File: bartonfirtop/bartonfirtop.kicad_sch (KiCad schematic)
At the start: 3 parts

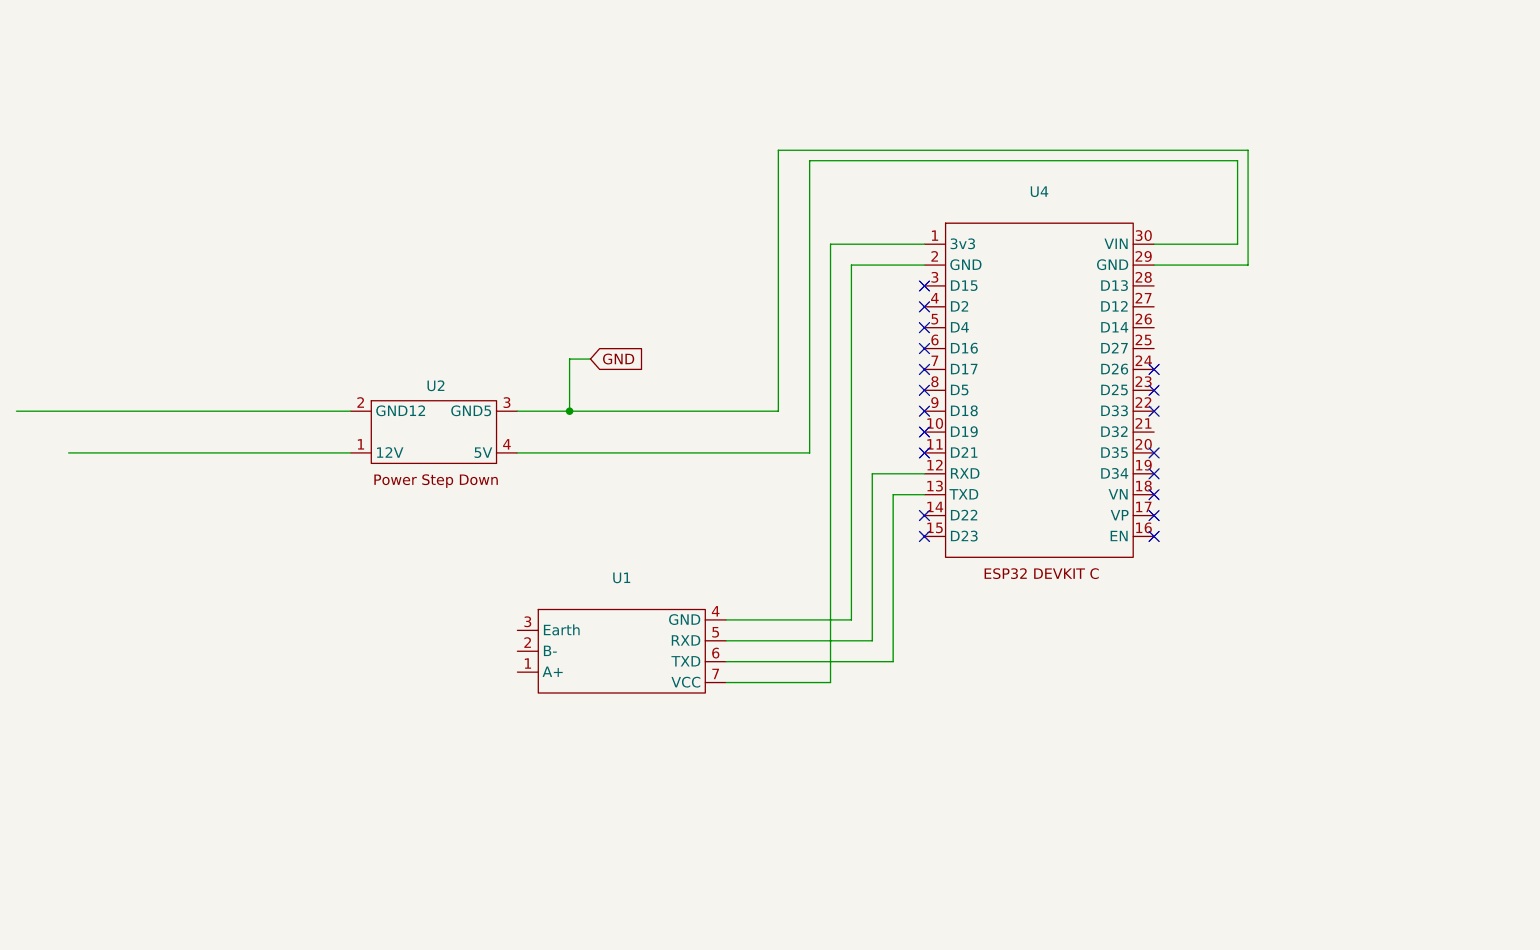
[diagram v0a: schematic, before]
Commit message: added LED connectors
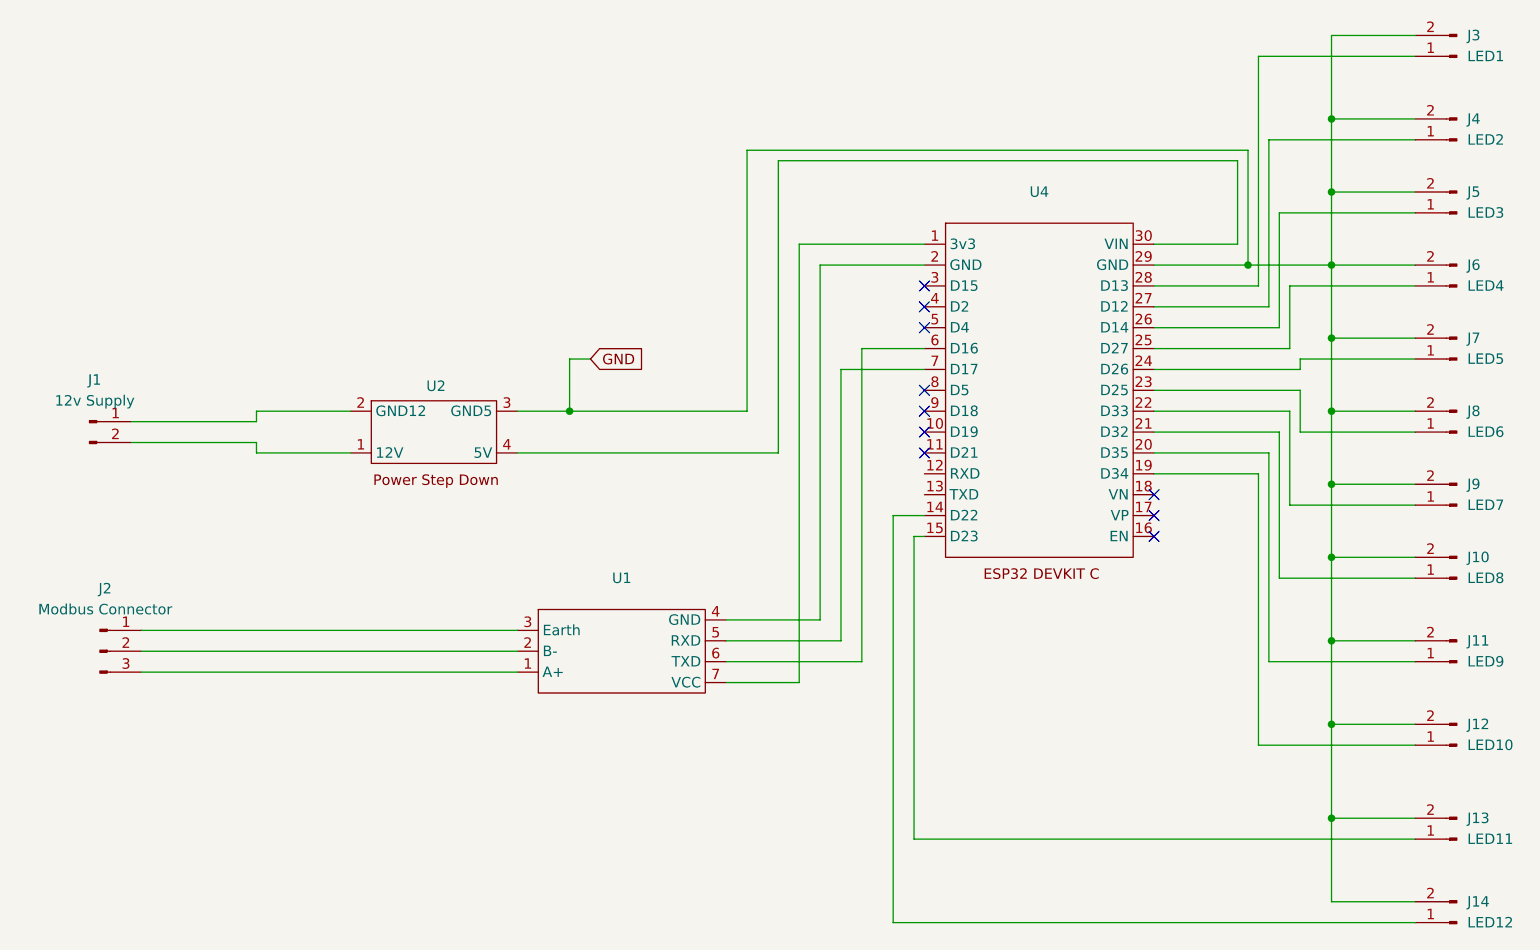
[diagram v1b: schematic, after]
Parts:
- added J1: 12v Supply, Connector_Molex:Molex_KK-254_AE-6410-02A_1x02_P2.54mm_Vertical, symbol Connector:Conn_01x02_Pin
- added J10: LED8, Connector_Molex:Molex_KK-254_AE-6410-02A_1x02_P2.54mm_Vertical, symbol Connector:Conn_01x02_Pin
- added J11: LED9, Connector_Molex:Molex_KK-254_AE-6410-02A_1x02_P2.54mm_Vertical, symbol Connector:Conn_01x02_Pin
- added J12: LED10, Connector_Molex:Molex_KK-254_AE-6410-02A_1x02_P2.54mm_Vertical, symbol Connector:Conn_01x02_Pin
- added J13: LED11, Connector_Molex:Molex_KK-254_AE-6410-02A_1x02_P2.54mm_Vertical, symbol Connector:Conn_01x02_Pin
- added J14: LED12, Connector_Molex:Molex_KK-254_AE-6410-02A_1x02_P2.54mm_Vertical, symbol Connector:Conn_01x02_Pin
- added J2: Modbus Connector, symbol Connector:Conn_01x03_Pin
- added J3: LED1, Connector_Molex:Molex_KK-254_AE-6410-02A_1x02_P2.54mm_Vertical, symbol Connector:Conn_01x02_Pin
- added J4: LED2, Connector_Molex:Molex_KK-254_AE-6410-02A_1x02_P2.54mm_Vertical, symbol Connector:Conn_01x02_Pin
- added J5: LED3, Connector_Molex:Molex_KK-254_AE-6410-02A_1x02_P2.54mm_Vertical, symbol Connector:Conn_01x02_Pin
- added J6: LED4, Connector_Molex:Molex_KK-254_AE-6410-02A_1x02_P2.54mm_Vertical, symbol Connector:Conn_01x02_Pin
- added J7: LED5, Connector_Molex:Molex_KK-254_AE-6410-02A_1x02_P2.54mm_Vertical, symbol Connector:Conn_01x02_Pin
- added J8: LED6, Connector_Molex:Molex_KK-254_AE-6410-02A_1x02_P2.54mm_Vertical, symbol Connector:Conn_01x02_Pin
- added J9: LED7, Connector_Molex:Molex_KK-254_AE-6410-02A_1x02_P2.54mm_Vertical, symbol Connector:Conn_01x02_Pin
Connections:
- net GND: now also J10.2 (Pin_2), J11.2 (Pin_2), J12.2 (Pin_2), J13.2 (Pin_2), J14.2 (Pin_2), J3.2 (Pin_2), J4.2 (Pin_2), J5.2 (Pin_2), J6.2 (Pin_2), J7.2 (Pin_2), J8.2 (Pin_2), J9.2 (Pin_2)
- net at U2.1 (12V): now also J1.2 (Pin_2)
- net at U2.2 (GND12): now also J1.1 (Pin_1)
- net at U4.12 (RXD): no longer U1.5 (RXD)
- net at U4.13 (TXD): no longer U1.6 (TXD)
- net at U4.14 (D22): now also J14.1 (Pin_1)
- net at U4.15 (D23): now also J13.1 (Pin_1)
- net at U4.19 (D34): now also J12.1 (Pin_1)
- net at U4.20 (D35): now also J11.1 (Pin_1)
- net at U4.21 (D32): now also J10.1 (Pin_1)
- net at U4.22 (D33): now also J9.1 (Pin_1)
- net at U4.23 (D25): now also J8.1 (Pin_1)
- net at U4.24 (D26): now also J7.1 (Pin_1)
- net at U4.25 (D27): now also J6.1 (Pin_1)
- net at U4.26 (D14): now also J5.1 (Pin_1)
- net at U4.27 (D12): now also J4.1 (Pin_1)
- net at U4.28 (D13): now also J3.1 (Pin_1)
- net at U4.6 (D16): now also U1.6 (TXD)
- net at U4.7 (D17): now also U1.5 (RXD)
- net at U1.1 (A+): now also J2.3 (Pin_3)
- net at U1.2 (B-): now also J2.2 (Pin_2)
- net at U1.3 (Earth): now also J2.1 (Pin_1)
- no-connect marks 19 -> 10

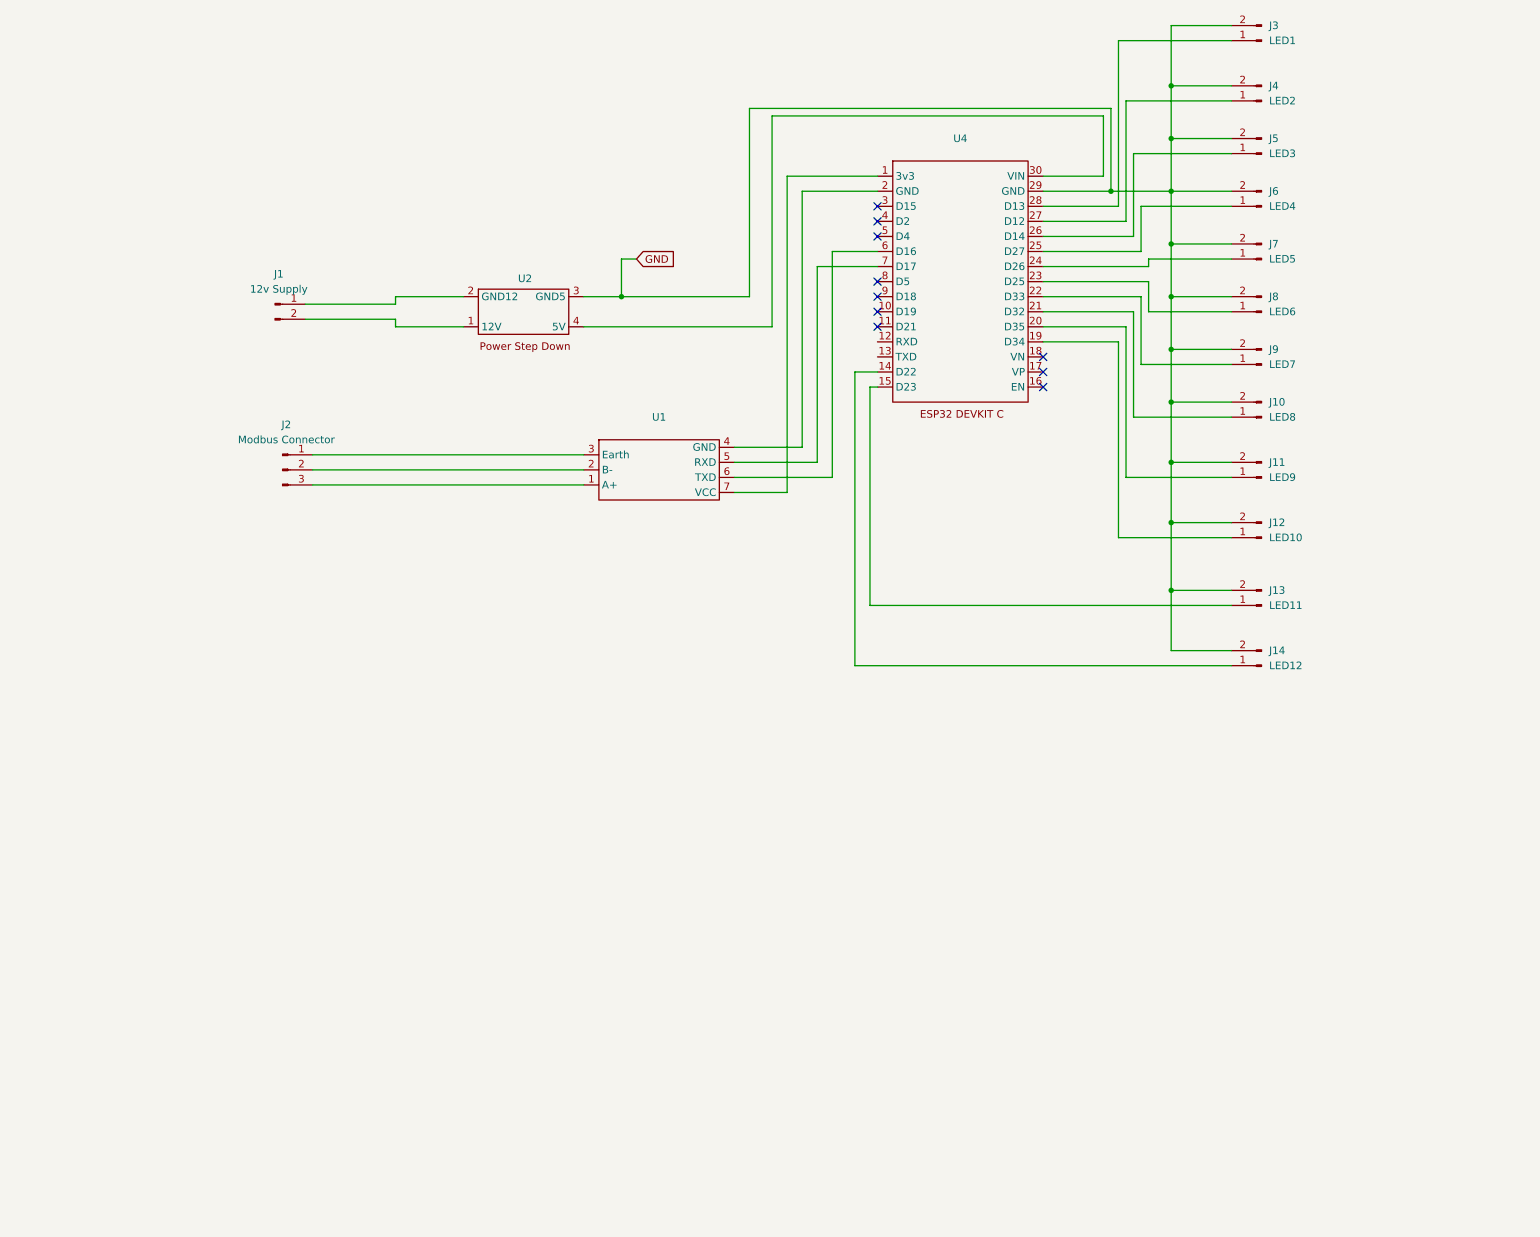
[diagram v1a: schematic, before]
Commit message: added switches and more LEDs
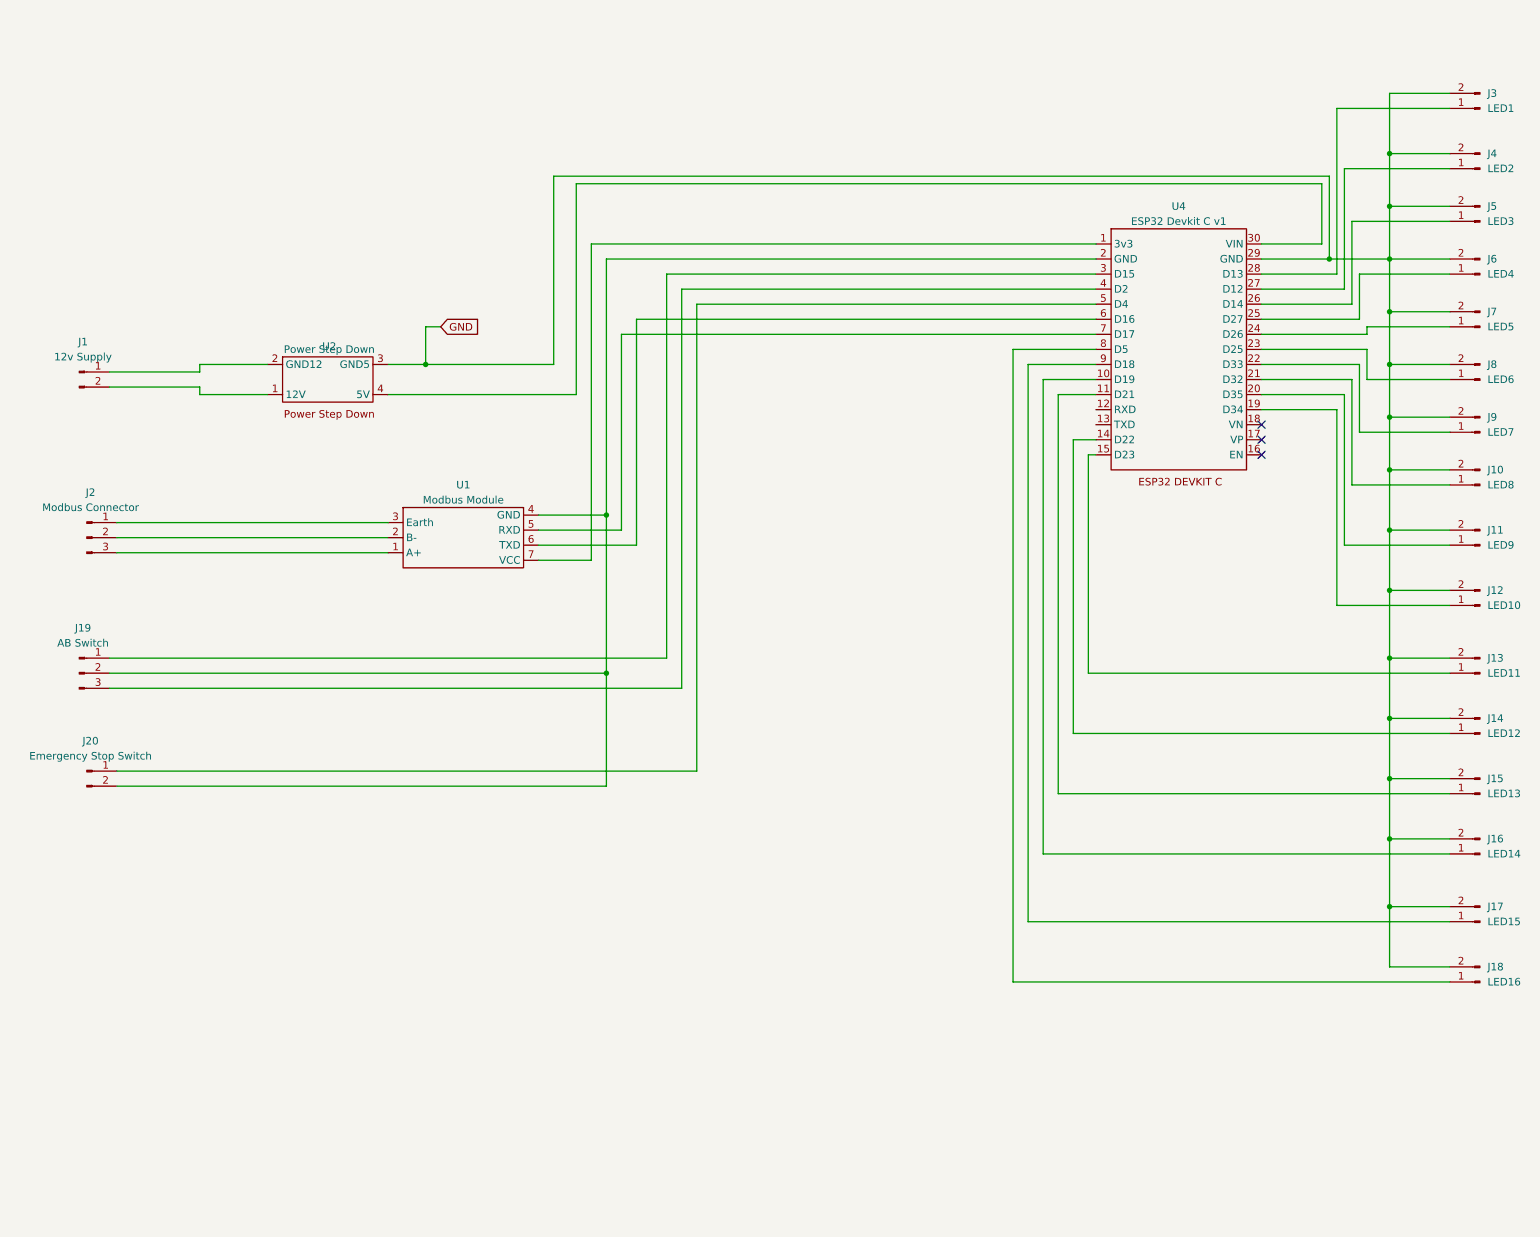
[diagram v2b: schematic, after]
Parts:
- added J15: LED13, Connector_Molex:Molex_KK-254_AE-6410-02A_1x02_P2.54mm_Vertical, symbol Connector:Conn_01x02_Pin
- added J16: LED14, Connector_Molex:Molex_KK-254_AE-6410-02A_1x02_P2.54mm_Vertical, symbol Connector:Conn_01x02_Pin
- added J17: LED15, Connector_Molex:Molex_KK-254_AE-6410-02A_1x02_P2.54mm_Vertical, symbol Connector:Conn_01x02_Pin
- added J18: LED16, Connector_Molex:Molex_KK-254_AE-6410-02A_1x02_P2.54mm_Vertical, symbol Connector:Conn_01x02_Pin
- added J19: AB Switch, Connector_Molex:Molex_KK-254_AE-6410-03A_1x03_P2.54mm_Vertical, symbol Connector:Conn_01x03_Pin
- added J20: Emergency Stop Switch, Connector_Molex:Molex_KK-254_AE-6410-02A_1x02_P2.54mm_Vertical, symbol Connector:Conn_01x02_Pin
- J2: footprint (none) -> Connector_Molex:Molex_KK-254_AE-6410-03A_1x03_P2.54mm_Vertical
- U1: value ~ -> Modbus Module
- U2: value ~ -> Power Step Down
- U4: value ~ -> ESP32 Devkit C v1
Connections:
- net GND: now also J15.2 (Pin_2), J16.2 (Pin_2), J17.2 (Pin_2), J18.2 (Pin_2)
- net at U4.10 (D19): now also J16.1 (Pin_1)
- net at U4.11 (D21): now also J15.1 (Pin_1)
- net at U1.4 (GND), U4.2 (GND): now also J19.2 (Pin_2), J20.2 (Pin_2)
- net at U4.3 (D15): now also J19.1 (Pin_1)
- net at U4.4 (D2): now also J19.3 (Pin_3)
- net at U4.5 (D4): now also J20.1 (Pin_1)
- net at U4.8 (D5): now also J18.1 (Pin_1)
- net at U4.9 (D18): now also J17.1 (Pin_1)
- no-connect marks 10 -> 3
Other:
- moved on the sheet: J1, J10, J11, J12, J13, J14, J2, J3, J4, J5, J6, J7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

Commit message: ordered 5 boards
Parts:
- U1: footprint (none) -> Library:Modbus Module
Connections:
- net GND: now also J19.2 (Pin_2), J20.2 (Pin_2), U1.4 (GND), U4.2 (GND)
- net at J15.1 (Pin_1): now also U4.8 (D5); no longer U4.11 (D21)
- net at J13.1 (Pin_1): now also U4.3 (D15); no longer U4.15 (D23)
- net at J19.1 (Pin_1): now also U4.14 (D22); no longer U4.3 (D15)
- net at J19.3 (Pin_3): now also U4.15 (D23); no longer U4.4 (D2)
- net at J16.1 (Pin_1): now also U4.9 (D18); no longer U4.10 (D19)
- net at J14.1 (Pin_1): now also U4.4 (D2); no longer U4.14 (D22)
- net at J18.1 (Pin_1): now also U4.11 (D21); no longer U4.8 (D5)
- net at J17.1 (Pin_1): now also U4.10 (D19); no longer U4.9 (D18)
- no-connect marks 3 -> 5
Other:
- moved on the sheet: J19

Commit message: testing 16 LEDs on the control board
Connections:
- net at J19.1 (Pin_1): now also U4.19 (D34); no longer U4.14 (D22)
- net at J19.3 (Pin_3): now also U4.20 (D35); no longer U4.15 (D23)
- net at J12.1 (Pin_1): now also U4.14 (D22); no longer U4.19 (D34)
- net at J11.1 (Pin_1): now also U4.15 (D23); no longer U4.20 (D35)
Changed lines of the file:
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@@
-	(wire
-		(pts
-			(xy 260.35 92.71) (xy 246.38 92.71)
-		)
-		(stroke
-			(width 0)
-			(type default)
-		)
-	)
 	(wire
 		(pts
@@
 	(wire
 		(pts
+			(xy 256.54 92.71) (xy 246.38 92.71)
+		)
+		(stroke
+			(width 0)
+			(type default)
+		)
+	)
+	(wire
+		(pts
+			(xy 205.74 128.27) (xy 278.13 128.27)
+		)
+		(stroke
+			(width 0)
+			(type default)
+		)
+	)
+	(wire
+		(pts
 			(xy 53.34 119.38) (xy 99.06 119.38)
 		)
@@
 	(wire
 		(pts
+			(xy 256.54 208.28) (xy 256.54 92.71)
+		)
+		(stroke
+			(width 0)
+			(type default)
+		)
+	)
+	(wire
+		(pts
 			(xy 278.13 137.16) (xy 267.97 137.16)
 		)
@@
 	(wire
 		(pts
+			(xy 252.73 95.25) (xy 246.38 95.25)
+		)
+		(stroke
+			(width 0)
+			(type default)
+		)
+	)
+	(wire
+		(pts
 			(xy 107.95 81.28) (xy 105.41 81.28)
 		)
@@
 	(wire
 		(pts
-			(xy 190.5 208.28) (xy 208.28 208.28)
+			(xy 190.5 208.28) (xy 256.54 208.28)
 		)
 		(stroke
@@
 	(wire
 		(pts
+			(xy 209.55 102.87) (xy 218.44 102.87)
+		)
+		(stroke
+			(width 0)
+			(type default)
+		)
+	)
+	(wire
+		(pts
 			(xy 67.31 88.9) (xy 67.31 87.63)
 		)
@@
 	(wire
 		(pts
-			(xy 208.28 102.87) (xy 218.44 102.87)
-		)
-		(stroke
-			(width 0)
-			(type default)
-		)
-	)
-	(wire
-		(pts
 			(xy 181.61 85.09) (xy 218.44 85.09)
 		)
@@
 	(wire
 		(pts
-			(xy 260.35 118.11) (xy 260.35 92.71)
-		)
-		(stroke
-			(width 0)
-			(type default)
-		)
-	)
-	(wire
-		(pts
 			(xy 278.13 41.91) (xy 267.97 41.91)
 		)
@@
 	(wire
 		(pts
-			(xy 259.08 95.25) (xy 246.38 95.25)
+			(xy 205.74 128.27) (xy 205.74 100.33)
 		)
 		(stroke
@@
 	(wire
 		(pts
-			(xy 278.13 118.11) (xy 260.35 118.11)
-		)
-		(stroke
-			(width 0)
-			(type default)
-		)
-	)
-	(wire
-		(pts
 			(xy 278.13 179.07) (xy 267.97 179.07)
 		)
@@
 	(wire
 		(pts
+			(xy 209.55 118.11) (xy 278.13 118.11)
+		)
+		(stroke
+			(width 0)
+			(type default)
+		)
+	)
+	(wire
+		(pts
 			(xy 218.44 72.39) (xy 146.05 72.39)
 		)
@@
 	(wire
 		(pts
+			(xy 205.74 100.33) (xy 218.44 100.33)
+		)
+		(stroke
+			(width 0)
+			(type default)
+		)
+	)
+	(wire
+		(pts
+			(xy 209.55 118.11) (xy 209.55 102.87)
+		)
+		(stroke
+			(width 0)
+			(type default)
+		)
+	)
+	(wire
+		(pts
 			(xy 278.13 99.06) (xy 262.89 99.06)
 		)
@@
 	(wire
 		(pts
-			(xy 205.74 203.2) (xy 205.74 100.33)
-		)
-		(stroke
-			(width 0)
-			(type default)
-		)
-	)
-	(wire
-		(pts
 			(xy 199.39 191.77) (xy 199.39 92.71)
 		)
@@
 	(wire
 		(pts
-			(xy 190.5 203.2) (xy 205.74 203.2)
+			(xy 190.5 203.2) (xy 252.73 203.2)
 		)
 		(stroke
@@
 	(wire
 		(pts
-			(xy 208.28 208.28) (xy 208.28 102.87)
-		)
-		(stroke
-			(width 0)
-			(type default)
-		)
-	)
-	(wire
-		(pts
-			(xy 205.74 100.33) (xy 218.44 100.33)
-		)
-		(stroke
-			(width 0)
-			(type default)
-		)
-	)
-	(wire
-		(pts
 			(xy 261.62 77.47) (xy 246.38 77.47)
 		)
@@
 	(wire
 		(pts
-			(xy 278.13 128.27) (xy 259.08 128.27)
-		)
-		(stroke
-			(width 0)
-			(type default)
-		)
-	)
-	(wire
-		(pts
-			(xy 259.08 128.27) (xy 259.08 95.25)
-		)
-		(stroke
-			(width 0)
-			(type default)
-		)
-	)
-	(wire
-		(pts
 			(xy 267.97 52.07) (xy 267.97 60.96)
 		)
 		(stroke
+			(width 0)
+			(type default)
+		)
+	)
+	(wire
+		(pts
+			(xy 252.73 203.2) (xy 252.73 95.25)
+		)
+		(stroke
